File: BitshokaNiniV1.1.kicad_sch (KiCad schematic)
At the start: 20 parts, among them J1 54-00164

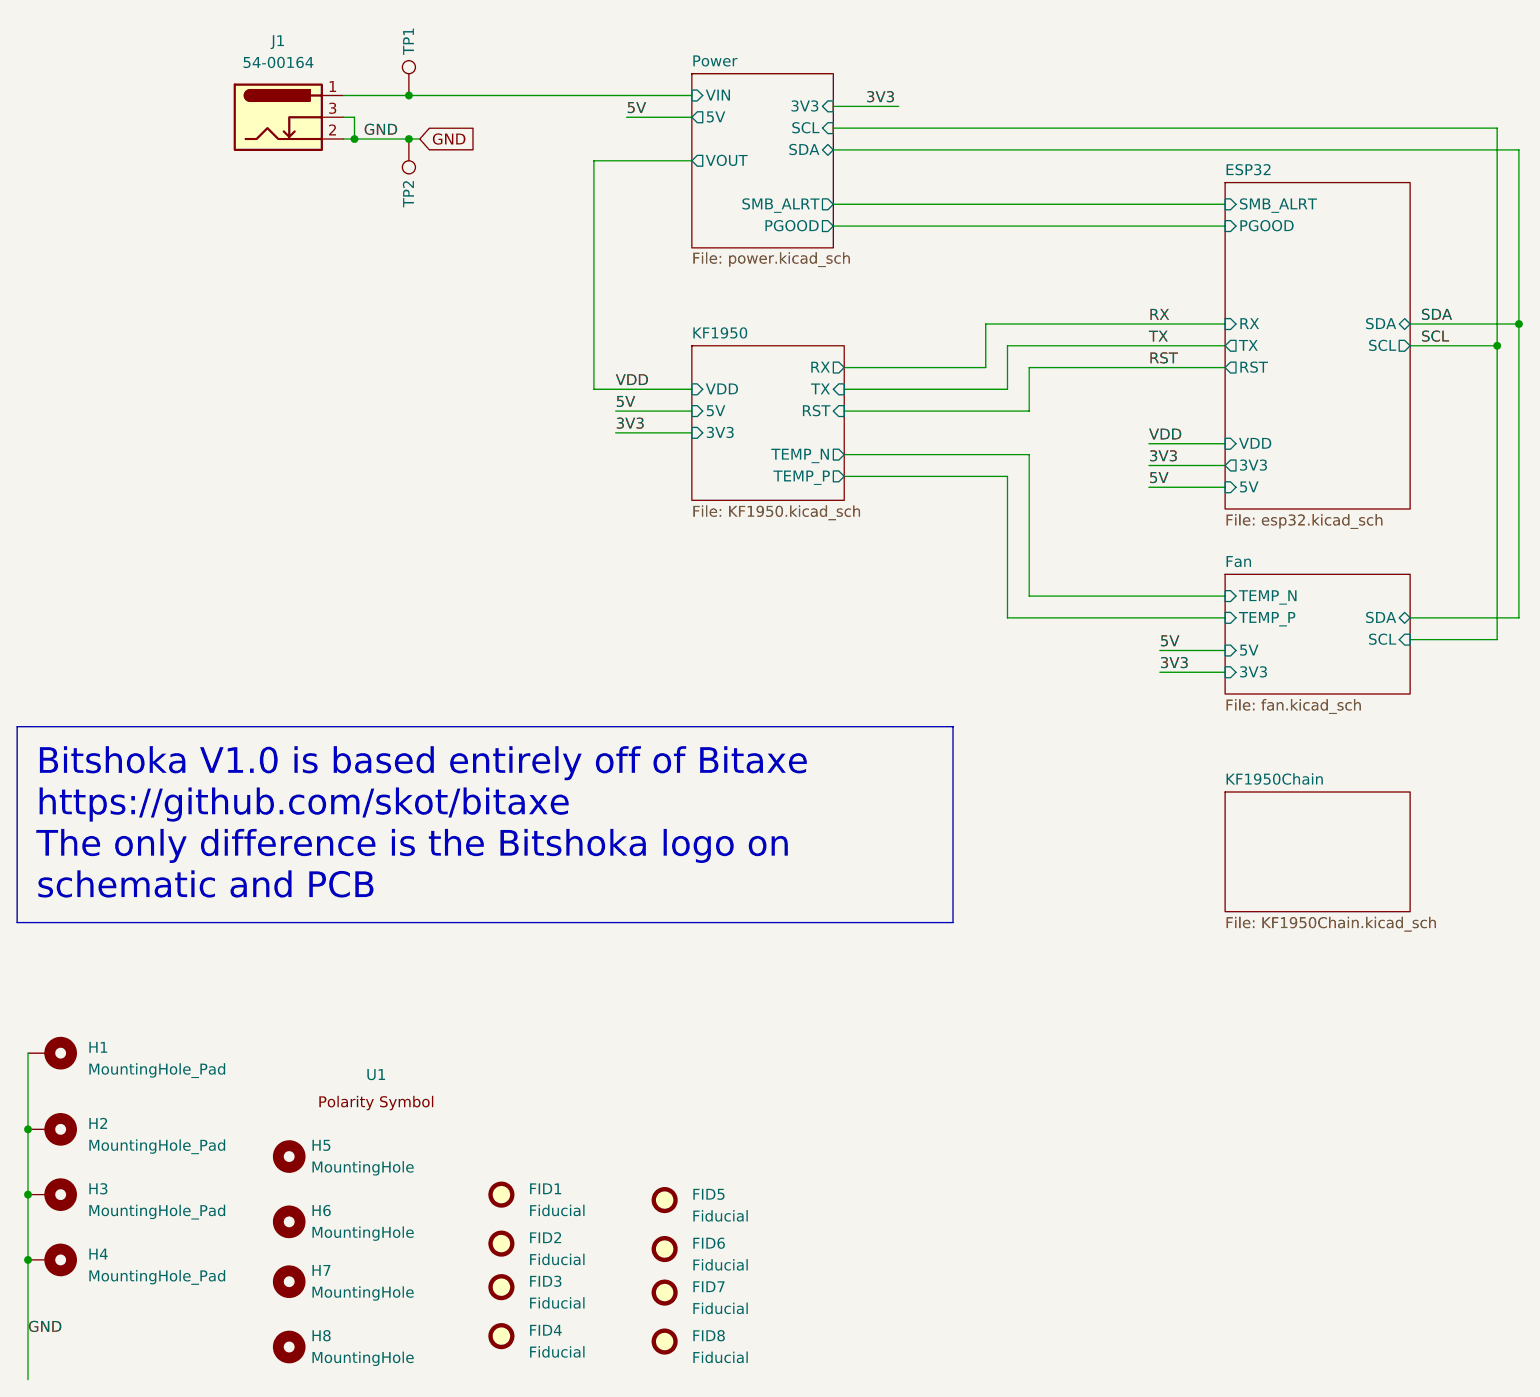
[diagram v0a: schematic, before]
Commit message: All components placed
Went through TI schematic and layout checklist.
All components placed and initial DRC
Need thermal vias on KF1950 and also better layout (so not so many errors)
Need to do silk
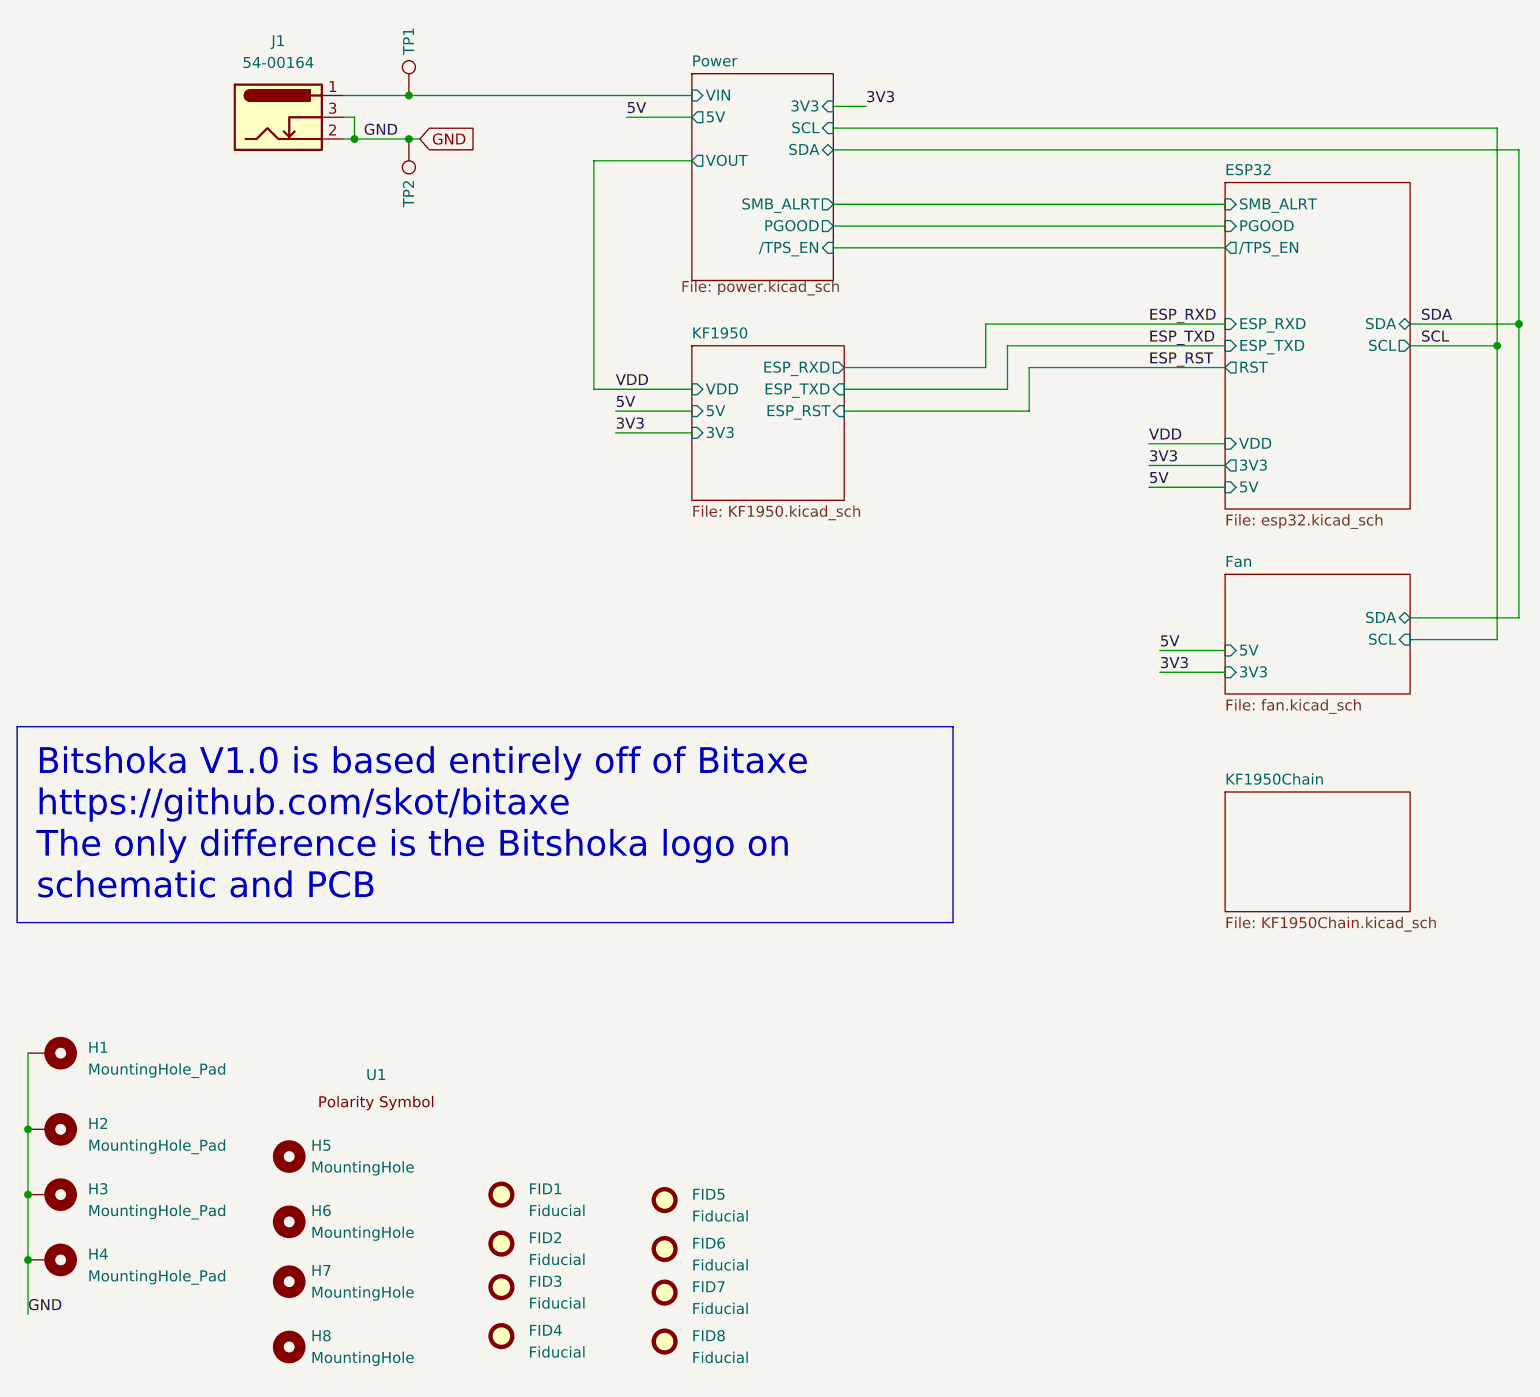
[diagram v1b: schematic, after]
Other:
- sheet ESP32 ports: added ESP_RXD, ESP_TXD, /TPS_EN; removed RX, TX
- sheet Fan ports: added none; removed TEMP_N, TEMP_P
- sheet KF1950 ports: added ESP_RST, ESP_RXD, ESP_TXD; removed RST, RX, TEMP_N, TEMP_P, TX
- sheet Power ports: added /TPS_EN; removed none
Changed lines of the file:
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@@
-	(wire
-		(pts
-			(xy 152.4 101.6) (xy 175.26 101.6)
-		)
-		(stroke
-			(width 0)
-			(type default)
-		)
-	)
 	(wire
 		(pts
@@
 	(wire
 		(pts
-			(xy 175.26 104.14) (xy 149.86 104.14)
-		)
-		(stroke
-			(width 0)
-			(type default)
-		)
-	)
-	(wire
-		(pts
 			(xy 152.4 74.93) (xy 175.26 74.93)
 		)
@@
 	(wire
 		(pts
-			(xy 130.81 85.09) (xy 152.4 85.09)
-		)
-		(stroke
-			(width 0)
-			(type default)
-		)
-	)
-	(wire
-		(pts
 			(xy 149.86 77.47) (xy 149.86 72.39)
 		)
@@
 	(wire
 		(pts
-			(xy 149.86 87.63) (xy 130.81 87.63)
-		)
-		(stroke
-			(width 0)
-			(type default)
-		)
-	)
-	(wire
-		(pts
 			(xy 209.55 104.14) (xy 209.55 69.85)
 		)
@@
 	(wire
 		(pts
-			(xy 35.56 179.07) (xy 35.56 193.04)
-		)
-		(stroke
-			(width 0)
-			(type default)
-		)
-	)
-	(wire
-		(pts
 			(xy 35.56 154.94) (xy 35.56 163.83)
 		)
@@
 	(wire
 		(pts
-			(xy 152.4 85.09) (xy 152.4 101.6)
+			(xy 35.56 179.07) (xy 35.56 185.42)
 		)
 		(stroke
@@
 	(wire
 		(pts
-			(xy 149.86 104.14) (xy 149.86 87.63)
-		)
-		(stroke
-			(width 0)
-			(type default)
-		)
-	)
-	(wire
-		(pts
-			(xy 129.54 44.45) (xy 137.16 44.45)
+			(xy 129.54 60.96) (xy 175.26 60.96)
+		)
+		(stroke
+			(width 0)
+			(type default)
+		)
+	)
+	(wire
+		(pts
+			(xy 129.54 44.45) (xy 133.35 44.45)
 		)
 		(stroke
@@
 		)
 	)
-	(label "RST"
+	(label "ESP_RST"
 		(at 166.37 74.93 0)
 		(effects
@@
 	)
 	(label "GND"
-		(at 35.56 187.96 0)
+		(at 35.56 185.42 0)
 		(effects
 			(font
@@
 		)
 	)
-	(label "RX"
+	(label "ESP_RXD"
 		(at 166.37 69.85 0)
 		(effects
@@
 		)
 	)
-	(label "TX"
+	(label "ESP_TXD"
 		(at 166.37 72.39 0)
 		(effects
@@
 			)
 		)
-		(pin "TX" input
-			(at 130.81 77.47 0)
-			(effects
-				(font
-					(size 1.27 1.27)
-				)
-				(justify right)
-			)
-		)
-		(pin "RX" output
-			(at 130.81 74.93 0)
-			(effects
-				(font
-					(size 1.27 1.27)
-				)
-				(justify right)
-			)
-		)
-		(pin "RST" input
-			(at 130.81 80.01 0)
-			(effects
-				(font
-					(size 1.27 1.27)
-				)
-				(justify right)
-			)
-		)
 		(pin "3V3" input
 			(at 113.03 82.55 180)
@@
 			)
 		)
+		(pin "ESP_RST" input
+			(at 130.81 80.01 0)
+			(effects
+				(font
+					(size 1.27 1.27)
+				)
+				(justify right)
+			)
+		)
+		(pin "ESP_RXD" output
+			(at 130.81 74.93 0)
+			(effects
+				(font
+					(size 1.27 1.27)
+				)
+				(justify right)
+			)
+		)
+		(pin "ESP_TXD" input
+			(at 130.81 77.47 0)
+			(effects
+				(font
+					(size 1.27 1.27)
+				)
+				(justify right)
+			)
+		)
 		(pin "VDD" input
 			(at 113.03 77.47 180)
@@
 				)
 				(justify left)
-			)
-		)
-		(pin "TEMP_N" output
-			(at 130.81 85.09 0)
-			(effects
-				(font
-					(size 1.27 1.27)
-				)
-				(justify right)
-			)
-		)
-		(pin "TEMP_P" output
-			(at 130.81 87.63 0)
-			(effects
-				(font
-					(size 1.27 1.27)
-				)
-				(justify right)
 			)
 		)
@@
 			)
 		)
-		(pin "TEMP_N" input
-			(at 175.26 101.6 180)
-			(effects
-				(font
-					(size 1.27 1.27)
-				)
-				(justify left)
-			)
-		)
-		(pin "TEMP_P" input
-			(at 175.26 104.14 180)
-			(effects
-				(font
-					(size 1.27 1.27)
-				)
-				(justify left)
-			)
-		)
 		(instances
 			(project "BitshokaNiniV1.1"
@@
 	(sheet
 		(at 113.03 40.64)
-		(size 16.51 20.32)
+		(size 16.51 24.13)
 		(exclude_from_sim no)
 		(in_bom yes)
@@
 		)
 		(property "Sheetfile" "power.kicad_sch"
-			(at 113.03 61.468 0)
+			(at 111.76 64.77 0)
 			(effects
 				(font
@@
 		(pin "SMB_ALRT" output
 			(at 129.54 55.88 0)
+			(effects
+				(font
+					(size 1.27 1.27)
+				)
+				(justify right)
+			)
+		)
+		(pin "{slash}TPS_EN" input
+			(at 129.54 60.96 0)
 			(effects
 				(font
@@
 			)
 		)
-		(pin "RX" input
-			(at 175.26 69.85 180)
-			(effects
-				(font
-					(size 1.27 1.27)
-				)
-				(justify left)
-			)
-		)
-		(pin "TX" output
-			(at 175.26 72.39 180)
-			(effects
-				(font
-					(size 1.27 1.27)
-				)
-				(justify left)
-			)
-		)
 		(pin "RST" output
 			(at 175.26 74.93 180)
@@
 			(effects
 				(font
+					(size 1.27 1.27)
+				)
+				(justify left)
+			)
+		)
+		(pin "ESP_RXD" input
+			(at 175.26 69.85 180)
+			(effects
+				(font
+					(size 1.27 1.27)
+				)
+				(justify left)
+			)
+		)
+		(pin "ESP_TXD" input
+			(at 175.26 72.39 180)
+			(effects
+				(font
+					(size 1.27 1.27)
+				)
+				(justify left)
+			)
+		)
+		(pin "{slash}TPS_EN" output
+			(at 175.26 60.96 180)
+			(effects
+				(font

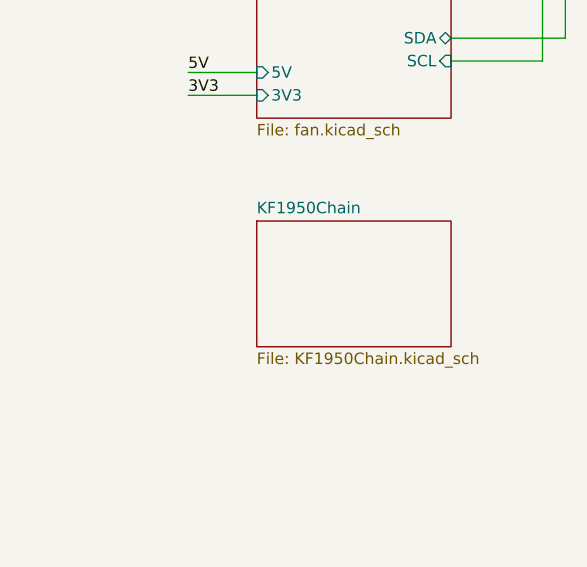
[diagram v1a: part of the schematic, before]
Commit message: PCB fixes
Fixed up KF1950 footprint
Added heatsinking to the bottom
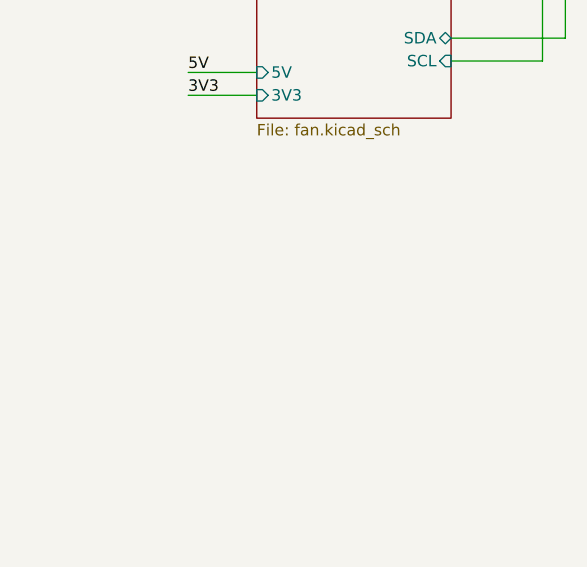
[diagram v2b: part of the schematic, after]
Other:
- removed sheet KF1950Chain
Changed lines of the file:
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@@
-	)
-	(sheet
-		(at 175.26 124.46)
-		(size 21.59 13.97)
-		(exclude_from_sim no)
-		(in_bom yes)
-		(on_board yes)
-		(dnp no)
-		(fields_autoplaced yes)
-		(stroke
-			(width 0.1524)
-			(type solid)
-		)
-		(fill
-			(color 0 0 0 0.0000)
-		)
-		(property "Sheetname" "KF1950Chain"
-			(at 175.26 123.7484 0)
-			(effects
-				(font
-					(size 1.27 1.27)
-				)
-				(justify left bottom)
-			)
-		)
-		(property "Sheetfile" "KF1950Chain.kicad_sch"
-			(at 175.26 139.0146 0)
-			(effects
-				(font
-					(size 1.27 1.27)
-				)
-				(justify left top)
-			)
-		)
-		(instances
-			(project "BitshokaNiniV1.1"
-				(path "/e63e39d7-6ac0-4ffd-8aa3-1841a4541b55"
-					(page "6")
-				)
-			)
-		)
 	)
 	(sheet

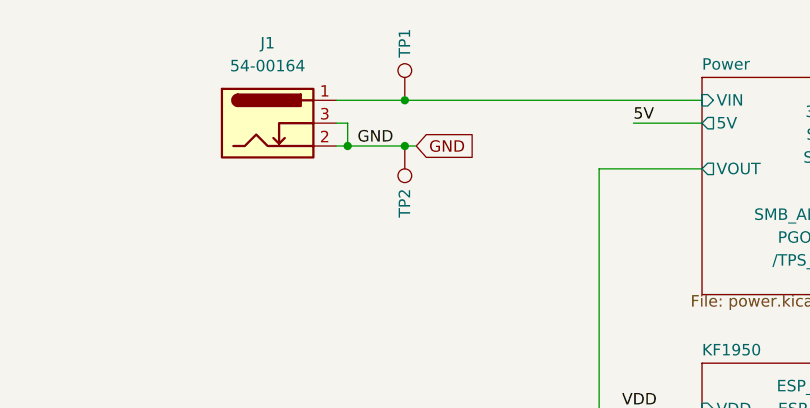
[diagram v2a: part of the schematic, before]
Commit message: Manfacturing prep
Add part numbers and did initial BOM optimization (Hope to do more after testing)
Created Manufacturing files
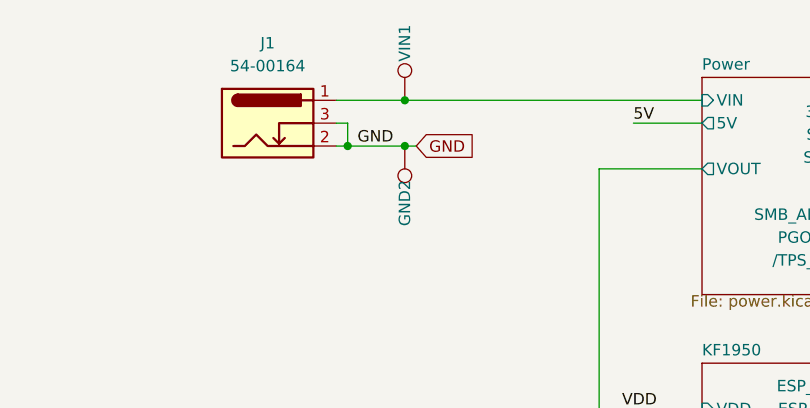
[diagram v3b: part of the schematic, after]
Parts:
- renumbered TP2 to GND2, TP1 to VIN1
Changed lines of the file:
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@@
 		(on_board yes)
 		(dnp no)
-		(property "Reference" "TP1"
+		(property "Reference" "VIN1"
 			(at 80.01 36.83 90)
 			(effects
@@
 			(project "bitaxeGamma"
 				(path "/e63e39d7-6ac0-4ffd-8aa3-1841a4541b55"
-					(reference "TP1")
+					(reference "VIN1")
 					(unit 1)
 				)
@@
 		(on_board yes)
 		(dnp no)
-		(property "Reference" "TP2"
+		(property "Reference" "GND2"
 			(at 80.01 54.61 90)
 			(effects
@@
 			(project "bitaxeGamma"
 				(path "/e63e39d7-6ac0-4ffd-8aa3-1841a4541b55"
-					(reference "TP2")
+					(reference "GND2")
 					(unit 1)
 				)

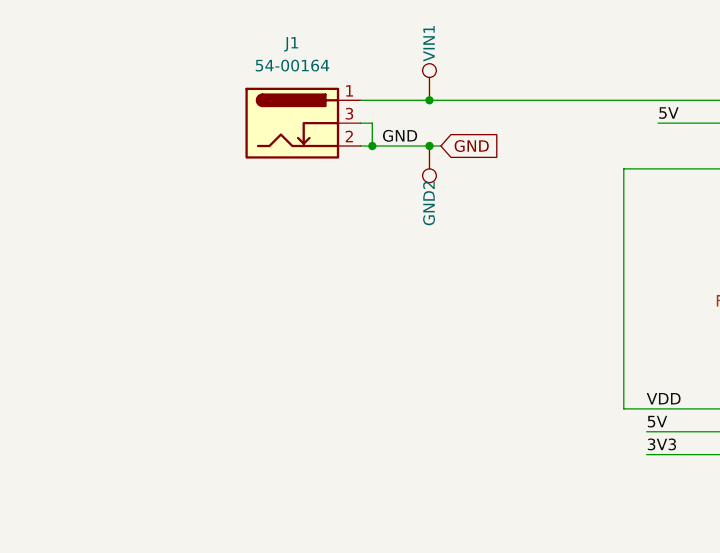
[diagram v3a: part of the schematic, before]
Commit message: Addressed Bitaxe Gamma Issues
- moved Fan caps
- added USB CC1 & CC2 pulldowns
- (I2C pullups were already done)
- reviewed but so far did not address any of the other issues/bugs
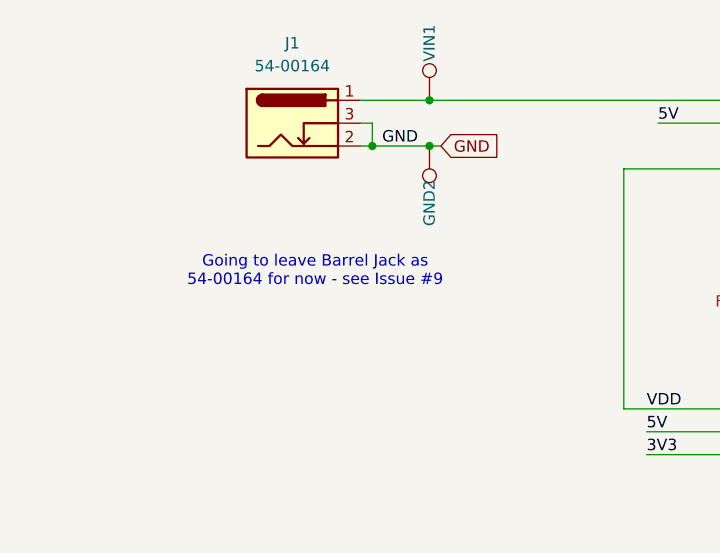
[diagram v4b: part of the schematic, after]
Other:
- note added: "Going to leave Barrel Jack as 54-00164 for now - see Issue #9"
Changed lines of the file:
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@@
 		(rev "601")
+	)
+	(text "Going to leave Barrel Jack as\n54-00164 for now - see Issue #9"
+		(exclude_from_sim no)
+		(at 67.31 62.23 0)
+		(effects
+			(font
+				(size 1.27 1.27)
+			)
+		)
 	)
 	(text_box "Bitshoka V1.0 is based entirely off of Bitaxe\nhttps://github.com/skot/bitaxe\nThe only difference is the Bitshoka logo on schematic and PCB\n"
